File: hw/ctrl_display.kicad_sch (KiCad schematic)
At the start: 27 parts

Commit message: add hw design for veraduino
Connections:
- net DEV0_~{CS} renamed VERA_~{CS}
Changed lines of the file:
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@@
     (effects (font (size 1.27 1.27)) (justify left bottom))
   )
-  (label "DEV0_~{CS}" (at 46.99 62.23 0) (fields_autoplaced)
+  (label "VERA_~{CS}" (at 46.99 62.23 0) (fields_autoplaced)
     (effects (font (size 1.27 1.27)) (justify left bottom))
   )

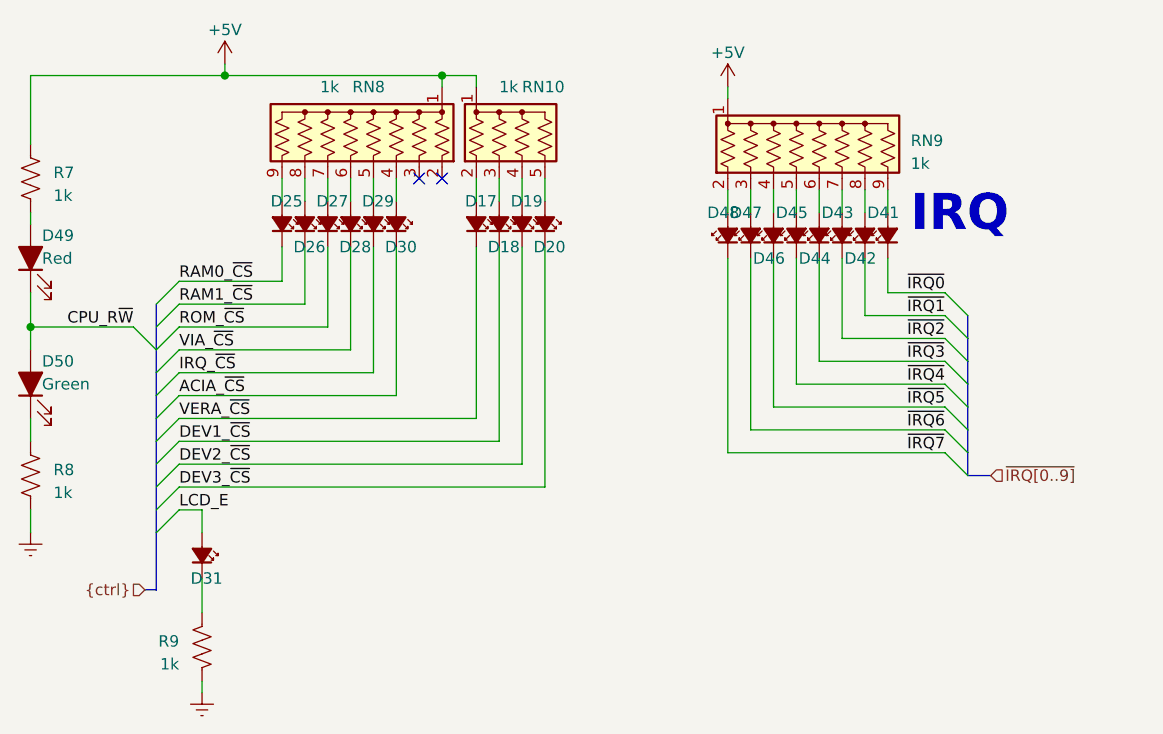
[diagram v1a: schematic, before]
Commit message: add hw schematics for video output with veraduino
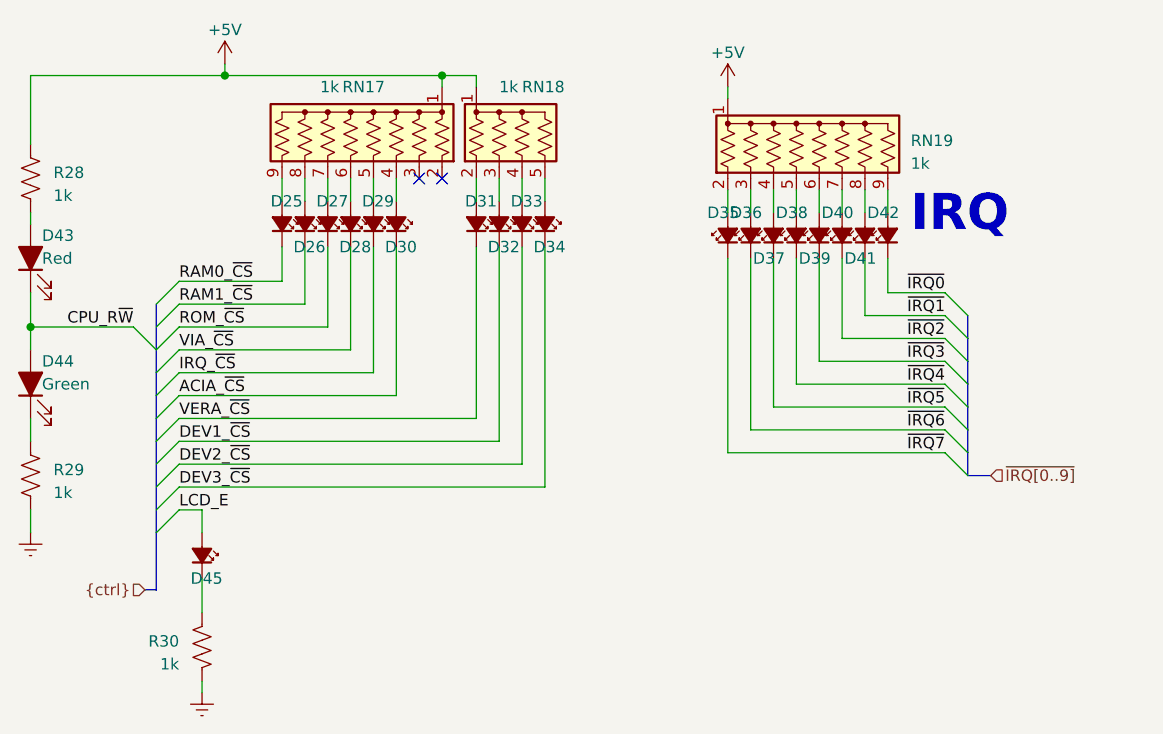
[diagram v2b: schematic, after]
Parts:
- renumbered D17 to D31, D18 to D32, D19 to D33, D20 to D34, D48 to D35, D47 to D36, D46 to D37, D45 to D38, D44 to D39, D43 to D40, D42 to D41, D41 to D42, D49 to D43, D50 to D44, D31 to D45, R7 to R28, R8 to R29, R9 to R30, RN8 to RN17, RN10 to RN18, RN9 to RN19
